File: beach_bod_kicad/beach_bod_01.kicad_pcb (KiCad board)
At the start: 2 copper layers, 78.2 x 29.2 mm, 74 parts, among them J1 Conn_01x01, J3 BNC5-J-P-GN-RA-BH2D, J4 Conn_01x01, J5 USB4085-GF-A_REVA4, J6 USB4085-GF-A_REVA4, Q1 AO3401A, U1 LTC6269, U2 LTC6268, U3 LM7301

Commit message: Layout Adjustments
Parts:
- C1, C16, C17, C24, C25, C27, C28, C6, C7: moved to F.Cu
- C30, C31, C32, C33, C34: footprint Capacitor_SMD:C_0805_2012Metric_Pad1.18x1.45mm_HandSolder -> Capacitor_SMD:C_1210_3225Metric_Pad1.33x2.70mm_HandSolder
- moved C34 24.7 mm to (134.6, 83.8), turned to -90 degrees
- moved D2 24.4 mm to (138.2, 101.6)
- moved C33 20.8 mm to (131.3, 83.8), turned to -90 degrees
- moved FB2 17.6 mm to (128.5, 83.3), turned to 90 degrees
- moved C17 11.9 mm to (107.4, 101.2)
- moved C27 9.98 mm to (133.9, 100.6), turned to -90 degrees
- moved R14 9.94 mm to (121.4, 94.7)
- moved C6 8.49 mm to (109.2, 101.2)
- moved C28 8.29 mm to (132.1, 100.6), turned to -90 degrees
- moved R22 8.09 mm to (128.0, 100.3), turned to 90 degrees
- moved C29 7.75 mm to (114.6, 90.0), turned to -90 degrees
- moved C24 7.46 mm to (129.4, 91.7), turned to 180 degrees
- moved C25 7.46 mm to (129.4, 93.5), turned to 180 degrees
- moved R2 7.11 mm to (124.7, 90.4), turned to 90 degrees
- moved R11 6.86 mm to (130.0, 96.8)
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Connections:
- C2 pad 2: Net-(C11-Pad2) -> Net-(C2-Pad2)
- J1 pad 1: Net-(J1-Pad1) -> Net-(C2-Pad2)
- R3 pad 1: Net-(C11-Pad2) -> Net-(C2-Pad2)
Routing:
- net greg: track 17.0 -> 0.00 mm, vias 1 -> 0
- net Net-(R27-Pad1): track 13.8 -> 0.00 mm, vias 2 -> 0
- net VCC: track 8.14 -> 0.44 mm, vias 1 -> 0
- net Net-(U1-Pad3): track 4.89 -> 0.43 mm
- net Net-(R1-Pad1): track 3.57 -> 0.00 mm
- net Net-(FB2-Pad2): track 9.26 -> 6.42 mm
- net GNDREF: track 1.54 -> 0.00 mm, vias 1 -> 0

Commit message: Initial Route
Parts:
- C26: moved to F.Cu
- moved C16 8.44 mm to (108.2, 91.4)
- moved U2 6.37 mm to (109.7, 94.5), turned to 0 degrees
- moved C26 3.49 mm to (135.6, 92.6)
- moved C22 1.82 mm to (120.2, 101.1), turned to -90 degrees
- moved R19 1.21 mm to (117.6, 101.1), turned to -90 degrees
- moved R2 0.76 mm to (125.5, 90.4)
- moved C2 0.51 mm to (145.5, 76.5)
- moved C21 0.51 mm to (145.6, 95.5)
- moved C5 0.51 mm to (145.5, 82.5)
- moved R18 0.51 mm to (149.9, 95.5)
- moved R3 0.51 mm to (149.9, 76.5)
- moved R6 0.51 mm to (149.9, 82.5)
- moved C18 0.51 mm to (145.5, 101.6)
- moved C19 0.51 mm to (145.6, 99.6)
- moved C20 0.51 mm to (145.5, 97.5)
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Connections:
- U3 pad 5: (no net) -> greg
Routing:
- net greg: track 0.00 -> 107.0 mm, vias 0 -> 5
- net VCC: track 0.44 -> 92.4 mm, vias 0 -> 7
- net GNDREF: track 0.00 -> 47.0 mm, vias 0 -> 10
- net V-: track 0.00 -> 42.4 mm, vias 0 -> 2
- net V+: track 0.00 -> 42.3 mm
- net cc1: track 0.00 -> 26.5 mm
- net Net-(C13-Pad2): track 0.00 -> 23.8 mm
- net Net-(C13-Pad1): track 0.00 -> 23.4 mm
- net cc2: track 0.00 -> 21.6 mm, vias 0 -> 1
- net Net-(C22-Pad1): track 0.00 -> 21.1 mm
- net Net-(C5-Pad1): track 0.00 -> 21.1 mm
- net Net-(R14-Pad2): track 0.00 -> 19.7 mm
- net Net-(C22-Pad2): track 0.00 -> 19.4 mm, vias 0 -> 2
- net Net-(C18-Pad1): track 0.00 -> 17.5 mm
- net Net-(C2-Pad2): track 0.00 -> 17.4 mm
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- added copper zone on B.Cu, net GNDREF
- added copper zone on B.Cu, net V-

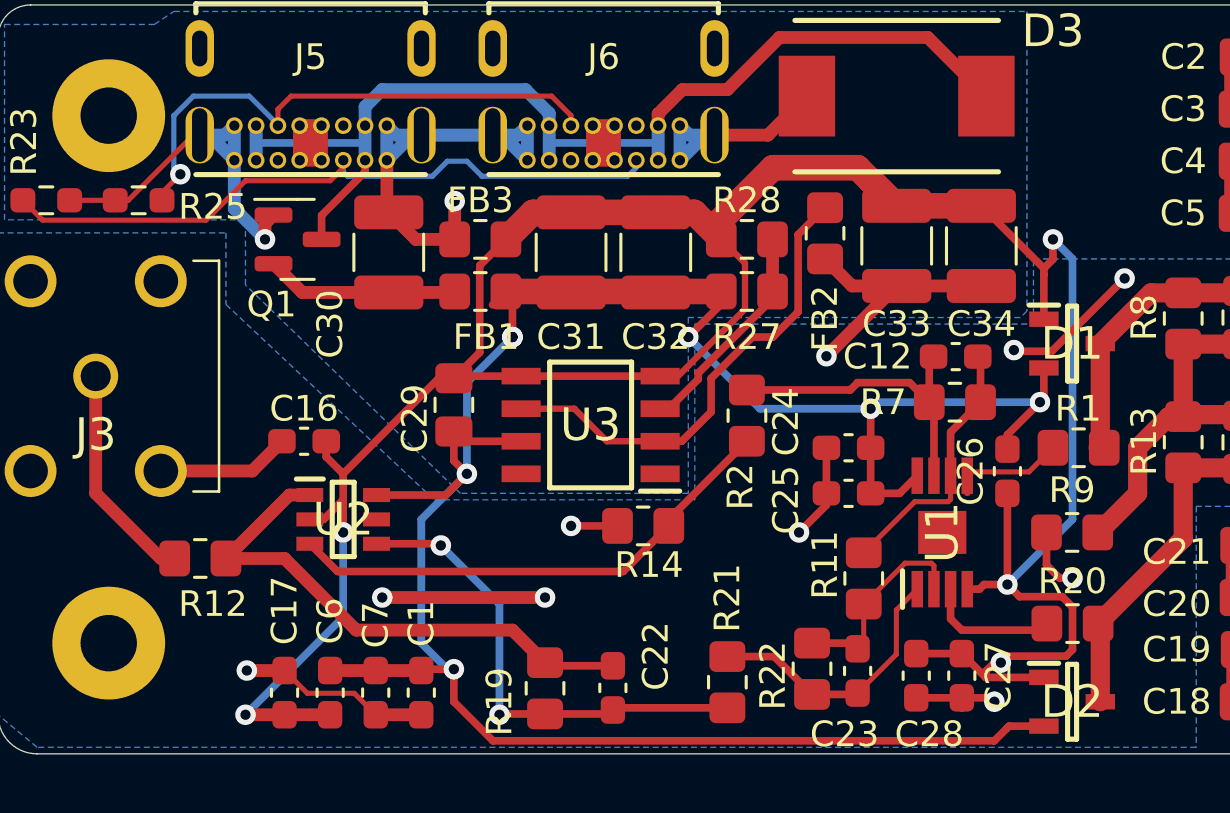
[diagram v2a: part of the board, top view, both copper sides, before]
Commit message: Reworked ground plane & output opamp
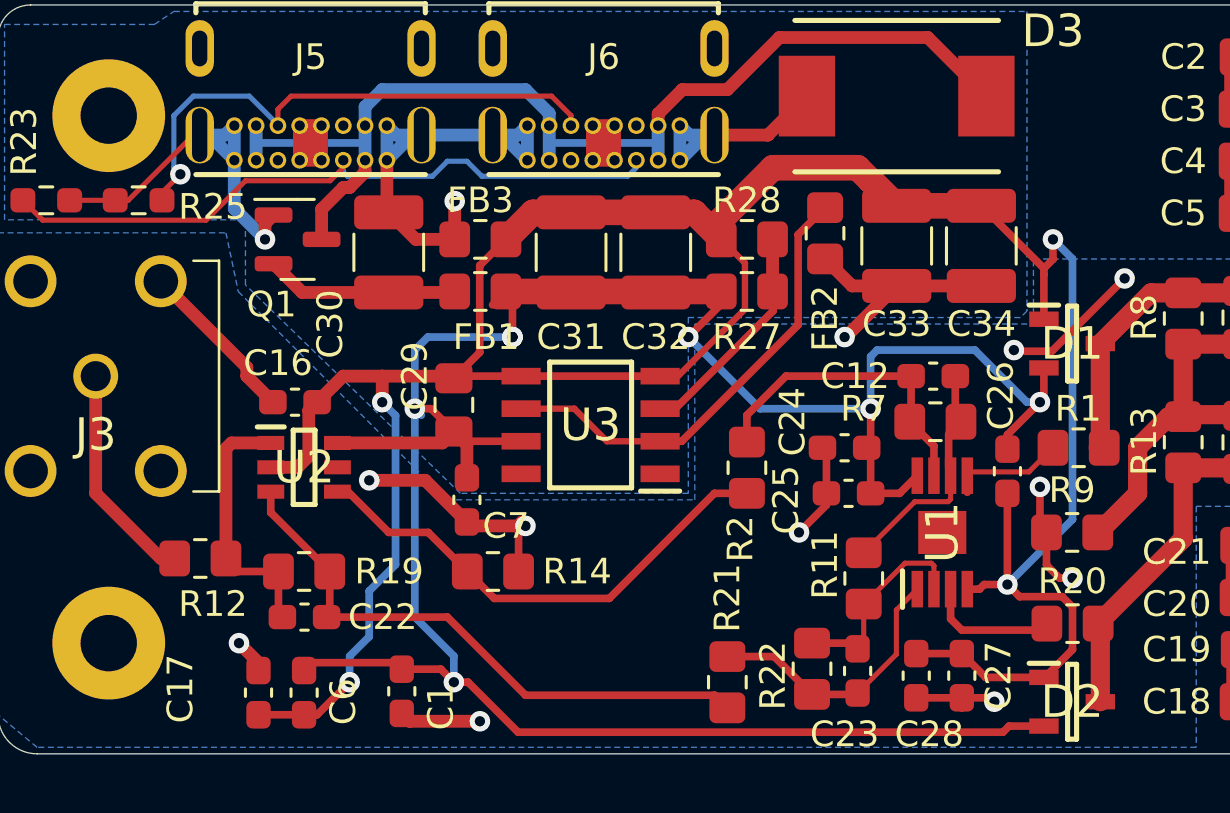
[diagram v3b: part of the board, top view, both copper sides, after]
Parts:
- moved C22 12.3 mm to (108.2, 98.3), turned to 0 degrees
- moved R19 10.4 mm to (108.2, 96.5), turned to 0 degrees
- moved C7 8.32 mm to (114.6, 93.7)
- moved R14 6.12 mm to (115.6, 96.5), turned to 180 degrees
- moved U2 2.54 mm to (108.2, 92.5)
- moved R2 2.03 mm to (125.5, 92.5)
- moved C16 1.56 mm to (107.8, 89.9)
- moved C12 1.16 mm to (132.7, 88.9)
- moved R7 1.08 mm to (132.8, 90.7)
- moved C6 1.02 mm to (108.2, 101.2)
- moved C17 1.02 mm to (106.4, 101.2)
- moved C1 0.76 mm to (112.0, 101.2)
- moved C24 0.15 mm to (129.3, 91.7)
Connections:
- U2 pad 3: Net-(R14-Pad2) -> Net-(C22-Pad2)
- U2 pad 4: Net-(C22-Pad2) -> Net-(R14-Pad2)
- U3 pad 5: greg -> (no net)
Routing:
- net Net-(C22-Pad1): track 21.1 -> 10.2 mm
- net VCC: track 92.4 -> 100.8 mm
- net Net-(C22-Pad2): track 19.4 -> 23.6 mm, vias 2 -> 0
- net Net-(C12-Pad2): track 10.5 -> 9.02 mm
- net greg: track 107.0 -> 108.0 mm, vias 5 -> 4
- net GNDREF: track 47.0 -> 46.6 mm, vias 10 -> 11

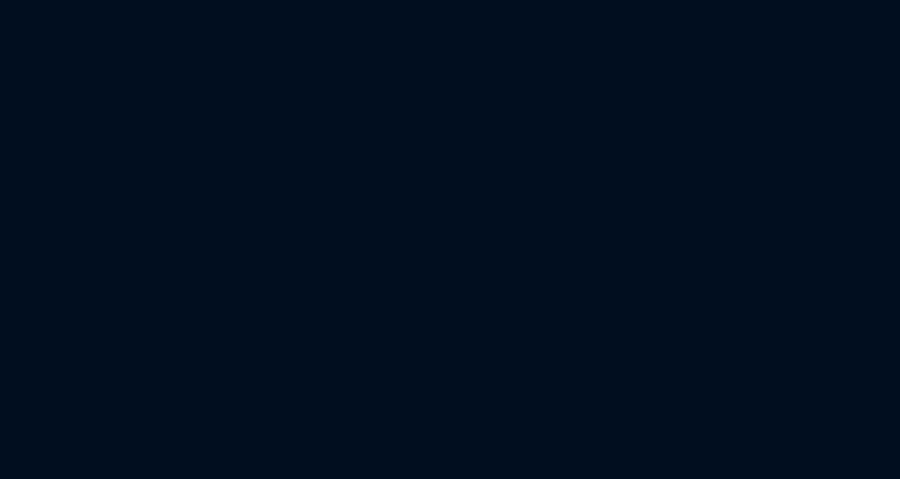
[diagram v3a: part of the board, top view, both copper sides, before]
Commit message: Added buds_diffprobe_spice and waveforms psu testing
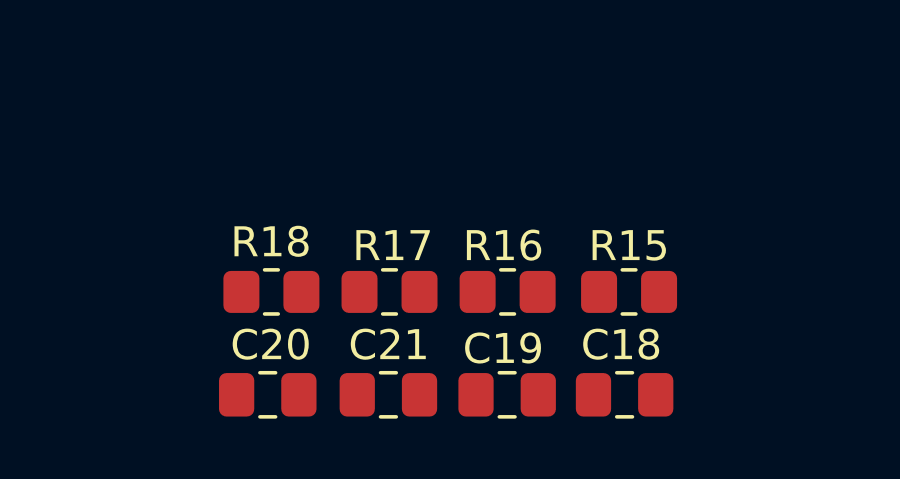
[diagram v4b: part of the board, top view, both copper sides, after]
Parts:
- added C18: 4pf, Capacitor_SMD:C_0805_2012Metric_Pad1.18x1.45mm_HandSolder, F.Cu at (153.2, 116.8)
- added C19: 4pf, Capacitor_SMD:C_0805_2012Metric_Pad1.18x1.45mm_HandSolder, F.Cu at (149.2, 116.8)
- added C20: 4pf, Capacitor_SMD:C_0805_2012Metric_Pad1.18x1.45mm_HandSolder, F.Cu at (145.3, 116.8)
- added C21: 4pf, Capacitor_SMD:C_0805_2012Metric_Pad1.18x1.45mm_HandSolder, F.Cu at (141.3, 116.8)
- added R15: 1M, Resistor_SMD:R_0805_2012Metric_Pad1.20x1.40mm_HandSolder, F.Cu at (153.3, 113.4)
- added R16: 1M, Resistor_SMD:R_0805_2012Metric_Pad1.20x1.40mm_HandSolder, F.Cu at (149.3, 113.4)
- added R17: 1M, Resistor_SMD:R_0805_2012Metric_Pad1.20x1.40mm_HandSolder, F.Cu at (145.3, 113.4)
- added R18: 1M, Resistor_SMD:R_0805_2012Metric_Pad1.20x1.40mm_HandSolder, F.Cu at (141.4, 113.4)
